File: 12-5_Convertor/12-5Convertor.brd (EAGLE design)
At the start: 29.1 x 41.3 mm, 14 parts, among them IC1 ACS764, U1 LM2678

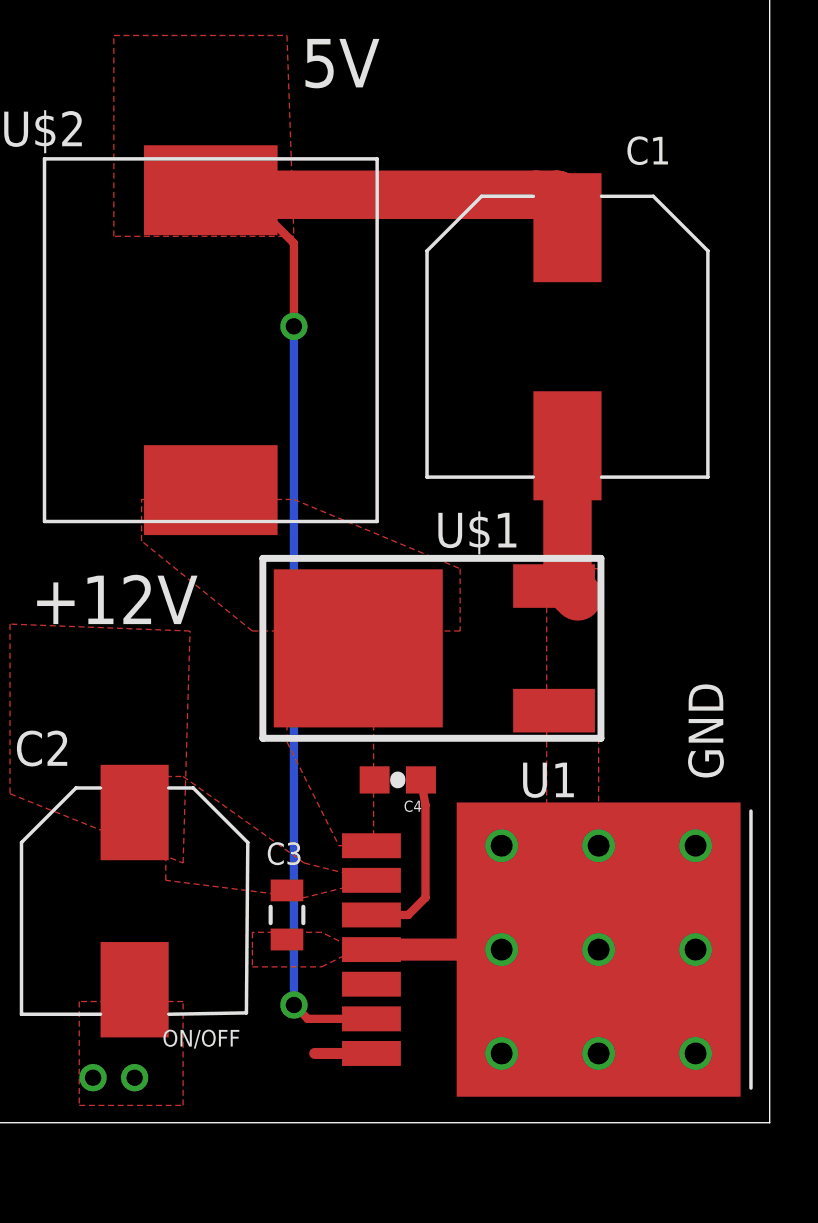
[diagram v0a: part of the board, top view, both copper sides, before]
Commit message: Cleaned up the buck regulator schematic
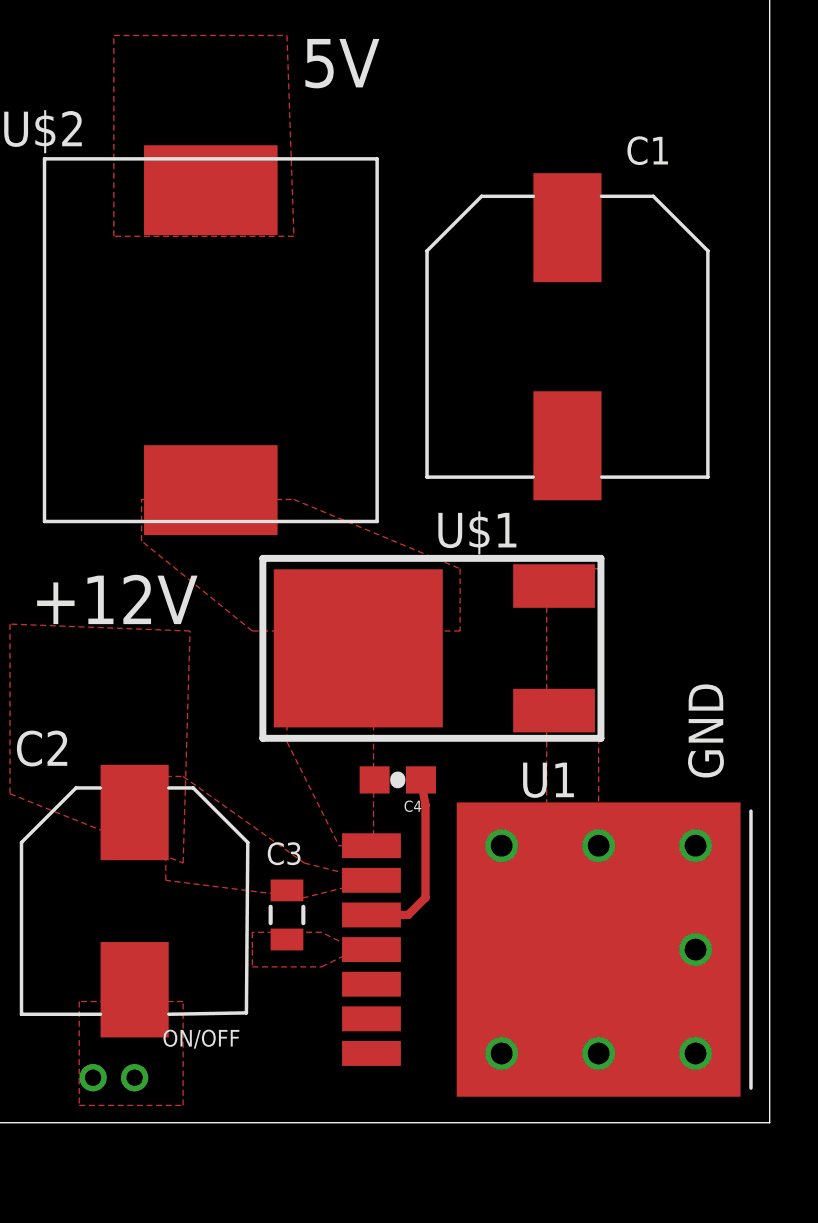
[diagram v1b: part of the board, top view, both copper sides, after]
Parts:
- C7, C8: value 10UF -> 1uF
- U$2: value HCMA1305 -> 22uH
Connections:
- removed net N$1: C8.1, R1.1, U$3.OUT
- new net N$5: R1.2, U1.7
- net +3V3: now also C8.1, R1.1, U$3.OUT; no longer R1.2, U1.7
- net +5V: no longer U1.6
- net VOUT: now also U1.6
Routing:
- net +5V: track 52.4 -> 0.00 mm, vias 2 -> 0
- net GND: track 10.5 -> 0.00 mm, vias 11 -> 9
- net +3V3: track 2.08 -> 0.00 mm

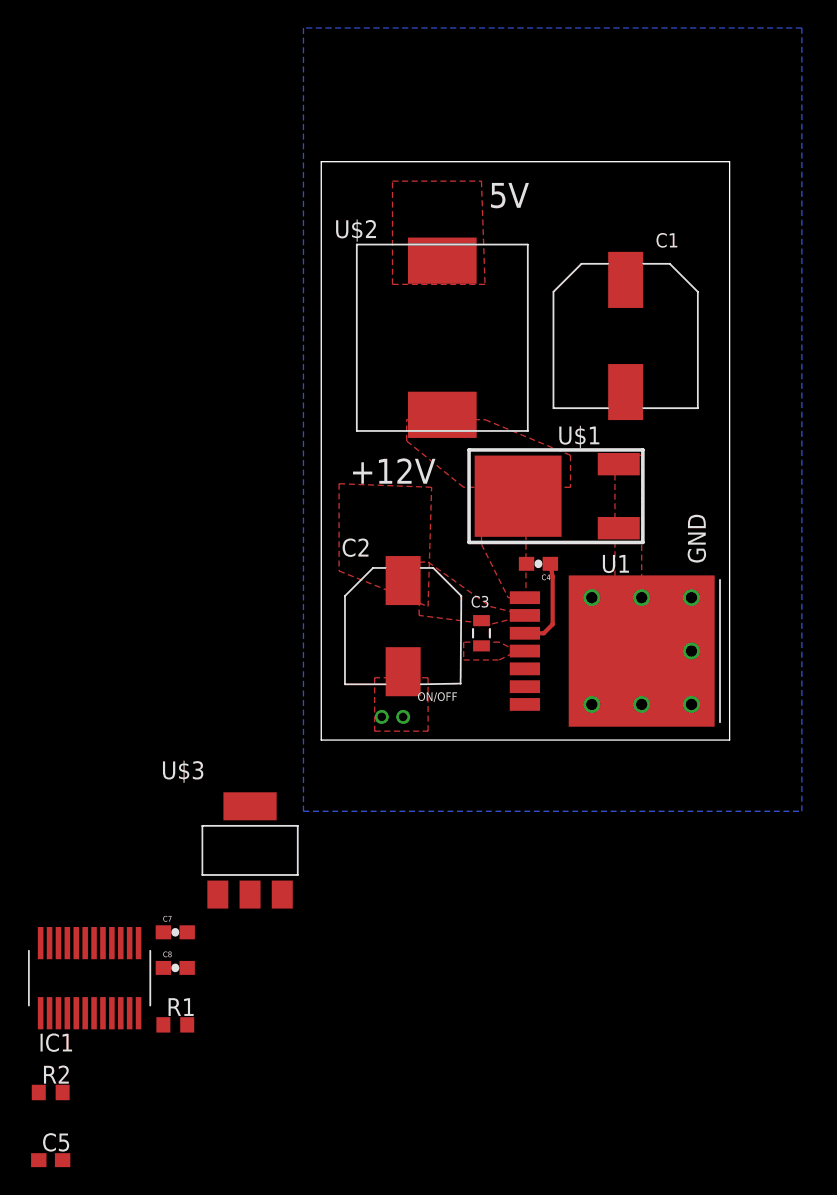
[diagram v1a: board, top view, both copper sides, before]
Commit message: ripped of wires in order to preapare for new board layout
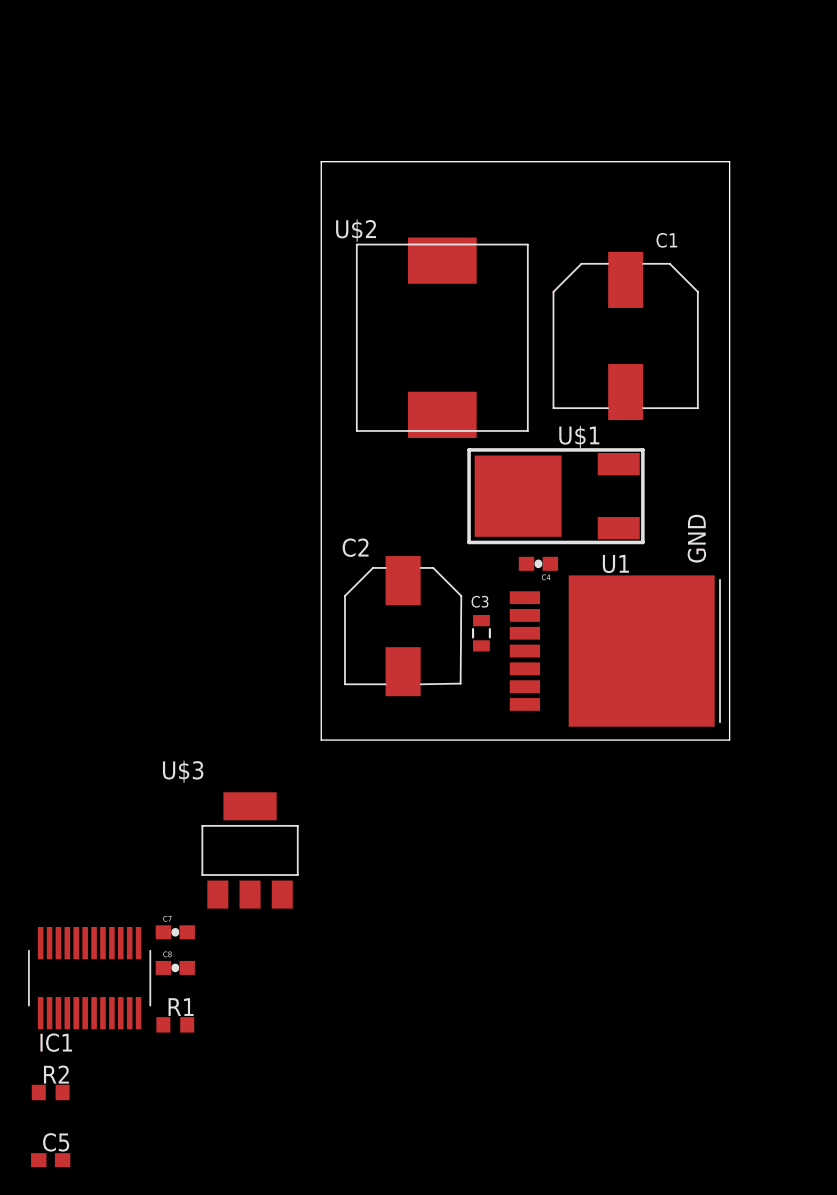
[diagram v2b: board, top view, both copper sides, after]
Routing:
- net N$2: track 6.58 -> 0.00 mm
- removed copper zone on layer 1, net +12V
- removed copper zone on layer 1, net +5V
- removed copper zone on layer 1, net GND
- removed copper zone on layer 16, net GND
- removed copper zone on layer 1, net N$3
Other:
- board text removed: "+12V"
- board text removed: "5V"
- board text removed: "ON/OFF"
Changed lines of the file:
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@@
 <?xml version="1.0" encoding="utf-8"?>
 <!DOCTYPE eagle SYSTEM "eagle.dtd">
-<eagle version="7.3.0">
+<eagle version="7.4.0">
 <drawing>
 <settings>
@@
 <grid distance="0.01" unitdist="inch" unit="inch" style="lines" multiple="1" display="yes" altdistance="0.025" altunitdist="inch" altunit="inch"/>
 <layers>
-<layer number="1" name="Top" color="4" fill="1" visible="no" active="yes"/>
-<layer number="16" name="Bottom" color="1" fill="1" visible="no" active="yes"/>
+<layer number="1" name="Top" color="4" fill="1" visible="yes" active="yes"/>
+<layer number="16" name="Bottom" color="1" fill="1" visible="yes" active="yes"/>
 <layer number="17" name="Pads" color="2" fill="1" visible="yes" active="yes"/>
 <layer number="18" name="Vias" color="2" fill="1" visible="yes" active="yes"/>
 <layer number="19" name="Unrouted" color="6" fill="1" visible="yes" active="yes"/>
 <layer number="20" name="Dimension" color="15" fill="1" visible="yes" active="yes"/>
-<layer number="21" name="tPlace" color="7" fill="1" visible="no" active="yes"/>
+<layer number="21" name="tPlace" color="7" fill="1" visible="yes" active="yes"/>
 <layer number="22" name="bPlace" color="7" fill="1" visible="yes" active="yes"/>
 <layer number="23" name="tOrigins" color="15" fill="1" visible="yes" active="yes"/>
@@
 <wire x1="60.884" y1="59.045" x2="31.75" y2="59.045" width="0" layer="20"/>
 <wire x1="31.75" y1="59.045" x2="31.75" y2="17.78" width="0" layer="20"/>
-<text x="33.782" y="36.068" size="1.778" layer="21">+12V</text>
-<text x="43.688" y="55.753" size="1.778" layer="21">5V</text>
 <text x="59.182" y="30.353" size="1.27" layer="21" rot="R90">GND</text>
-<text x="38.608" y="20.574" size="0.6096" layer="21">ON/OFF</text>
 <text x="37.846" y="54.102" size="1.016" layer="22" rot="MR180">Designed by Luke McBee,
 Richard Shen, Jeff Geiss,
@@
 <contactref element="U1" pad="3"/>
 <contactref element="C4" pad="1"/>
-<wire x1="46.2788" y1="25.4" x2="47.625" y2="25.4" width="0.3048" layer="1"/>
-<wire x1="47.625" y1="25.4" x2="48.26" y2="26.035" width="0.3048" layer="1"/>
-<wire x1="48.26" y1="26.035" x2="48.26" y2="29.425" width="0.3048" layer="1"/>
-<wire x1="48.26" y1="29.425" x2="48.094" y2="30.353" width="0.3048" layer="1"/>
+<wire x1="46.2788" y1="25.4" x2="48.094" y2="30.353" width="0" layer="19" extent="1-1"/>
 </signal>
 <signal name="N$3">
 <contactref element="C4" pad="2"/>
-<polygon width="0.4064" layer="1" thermals="no">
-<vertex x="43.18" y="31.75"/>
-<vertex x="45.085" y="27.94"/>
-<vertex x="46.355" y="27.94"/>
-<vertex x="46.355" y="32.385"/>
-<vertex x="43.18" y="32.385"/>
-</polygon>
-<polygon width="0.254" layer="1" thermals="no">
-<vertex x="37.846" y="40.64"/>
-<vertex x="43.434" y="40.64"/>
-<vertex x="49.53" y="38.1"/>
-<vertex x="49.53" y="35.814"/>
-<vertex x="41.91" y="35.814"/>
-<vertex x="37.846" y="39.116"/>
-</polygon>
 <contactref element="U1" pad="1"/>
 <contactref element="U$2" pad="P$1"/>
 <contactref element="U$1" pad="P$4"/>
-<wire x1="45.795" y1="35.179" x2="40.386" y2="40.982" width="0" layer="19" extent="1-1"/>
-<wire x1="46.394" y1="30.353" x2="45.795" y2="35.179" width="0" layer="19" extent="1-1"/>
-<wire x1="46.2788" y1="27.94" x2="46.394" y2="30.353" width="0" layer="19" extent="1-1"/>
 </signal>
 <signal name="GND">
-<via x="51.054" y="20.32" extent="1-16" drill="0.8"/>
-<via x="51.054" y="27.94" extent="1-16" drill="0.8"/>
-<via x="54.61" y="20.32" extent="1-16" drill="0.8"/>
-<via x="58.166" y="20.32" extent="1-16" drill="0.8"/>
-<via x="58.166" y="24.13" extent="1-16" drill="0.8"/>
-<via x="58.166" y="27.94" extent="1-16" drill="0.8"/>
-<via x="54.61" y="27.94" extent="1-16" drill="0.8"/>
-<via x="36.068" y="19.431" extent="1-16" drill="0.6"/>
-<polygon width="0.3048" layer="16">
-<vertex x="30.48" y="12.7"/>
-<vertex x="66.04" y="12.7"/>
-<vertex x="66.04" y="68.58"/>
-<vertex x="30.48" y="68.58"/>
-</polygon>
-<polygon width="0.3048" layer="1" thermals="no">
-<vertex x="52.705" y="38.1"/>
-<vertex x="52.705" y="29.21"/>
-<vertex x="54.61" y="29.21"/>
-<vertex x="54.61" y="38.1"/>
-</polygon>
-<polygon width="0.3048" layer="1" thermals="no">
-<vertex x="45.72" y="24.13"/>
-<vertex x="44.45" y="24.765"/>
-<vertex x="41.91" y="24.765"/>
-<vertex x="41.91" y="24.13"/>
-<vertex x="41.91" y="23.495"/>
-<vertex x="44.45" y="23.495"/>
-</polygon>
-<polygon width="0.3048" layer="1" thermals="no">
-<vertex x="35.56" y="22.225"/>
-<vertex x="35.56" y="18.415"/>
-<vertex x="39.37" y="18.415"/>
-<vertex x="39.37" y="22.225"/>
-</polygon>
-<via x="37.592" y="19.431" extent="1-16" drill="0.6"/>
 <contactref element="C7" pad="2"/>
 <contactref element="C8" pad="2"/>
@@
 <contactref element="IC1" pad="17"/>
 <wire x1="52.975" y1="37.464" x2="53.467" y2="42.609" width="0" layer="19" extent="1-1"/>
-<wire x1="52.975" y1="32.894" x2="52.975" y2="37.464" width="0" layer="19" extent="1-1"/>
-<wire x1="54.61" y1="27.94" x2="52.975" y2="32.894" width="0" layer="19" extent="1-1"/>
-<wire x1="58.166" y1="27.94" x2="54.61" y2="27.94" width="0" layer="19" extent="1-1"/>
-<wire x1="51.054" y1="27.94" x2="54.61" y2="27.94" width="0" layer="19" extent="1-1"/>
-<wire x1="58.166" y1="24.13" x2="58.166" y2="27.94" width="0" layer="19" extent="1-1"/>
-<wire x1="54.61" y1="24.13" x2="58.166" y2="24.13" width="0" layer="19" extent="1-1"/>
-<wire x1="58.166" y1="20.32" x2="58.166" y2="24.13" width="0" layer="19" extent="1-1"/>
-<wire x1="54.61" y1="20.32" x2="58.166" y2="20.32" width="0" layer="19" extent="1-1"/>
-<wire x1="51.054" y1="20.32" x2="54.61" y2="20.32" width="0" layer="19" extent="1-1"/>
-<wire x1="46.2788" y1="24.13" x2="51.054" y2="27.94" width="0" layer="19" extent="1-1"/>
+<wire x1="46.2788" y1="24.13" x2="54.61" y2="24.13" width="0" layer="19" extent="1-1"/>
 <wire x1="43.18" y1="24.5" x2="46.2788" y2="24.13" width="0" layer="19" extent="1-1"/>
 <wire x1="37.592" y1="22.658" x2="43.18" y2="24.5" width="0" layer="19" extent="1-1"/>
-<wire x1="37.592" y1="19.431" x2="37.592" y2="22.658" width="0" layer="19" extent="1-1"/>
-<wire x1="36.068" y1="19.431" x2="37.592" y2="19.431" width="0" layer="19" extent="1-1"/>
-<wire x1="24.37" y1="6.756" x2="36.068" y2="19.431" width="0" layer="19" extent="1-1"/>
+<wire x1="24.37" y1="6.756" x2="37.592" y2="22.658" width="0" layer="19" extent="1-1"/>
 <wire x1="22.186" y1="4.064" x2="24.37" y2="6.756" width="0" layer="19" extent="1-1"/>
 <wire x1="22.186" y1="1.524" x2="22.186" y2="4.064" width="0" layer="19" extent="1-1"/>
@@
 </signal>
 <signal name="+12V">
-<polygon width="0.254" layer="1" thermals="no">
-<vertex x="39.37" y="30.48"/>
-<vertex x="43.815" y="27.305"/>
-<vertex x="46.355" y="26.67"/>
-<vertex x="43.815" y="26.035"/>
-<vertex x="38.735" y="26.67"/>
-<vertex x="38.735" y="30.48"/>
-</polygon>
-<polygon width="0.254" layer="1" thermals="no">
-<vertex x="39.37" y="27.305"/>
-<vertex x="39.624" y="35.814"/>
-<vertex x="33.02" y="36.068"/>
-<vertex x="33.02" y="29.845"/>
-</polygon>
 <contactref element="U$3" pad="INPUT"/>
 <contactref element="C7" pad="1"/>
@@
 <contactref element="U1" pad="2"/>
 <contactref element="C3" pad="1"/>
-<wire x1="43.18" y1="26.3" x2="46.2788" y2="26.67" width="0" layer="19" extent="1-1"/>
-<wire x1="37.592" y1="29.158" x2="43.18" y2="26.3" width="0" layer="19" extent="1-1"/>
-<wire x1="28.97" y1="6.756" x2="37.592" y2="29.158" width="0" layer="19" extent="1-1"/>
 <wire x1="20.486" y1="4.064" x2="28.97" y2="6.756" width="0" layer="19" extent="1-1"/>
+<wire x1="37.592" y1="29.158" x2="28.97" y2="6.756" width="0" layer="19" extent="1-1"/>
 </signal>
 <signal name="+5V">
-<polygon width="0.3048" layer="1" thermals="no">
-<vertex x="36.83" y="57.658"/>
-<vertex x="43.18" y="57.658"/>
-<vertex x="43.434" y="50.292"/>
-<vertex x="36.83" y="50.292"/>
-</polygon>
 <contactref element="IC1" pad="19"/>
 <contactref element="IC1" pad="18"/>

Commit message: Updated the power conversion board
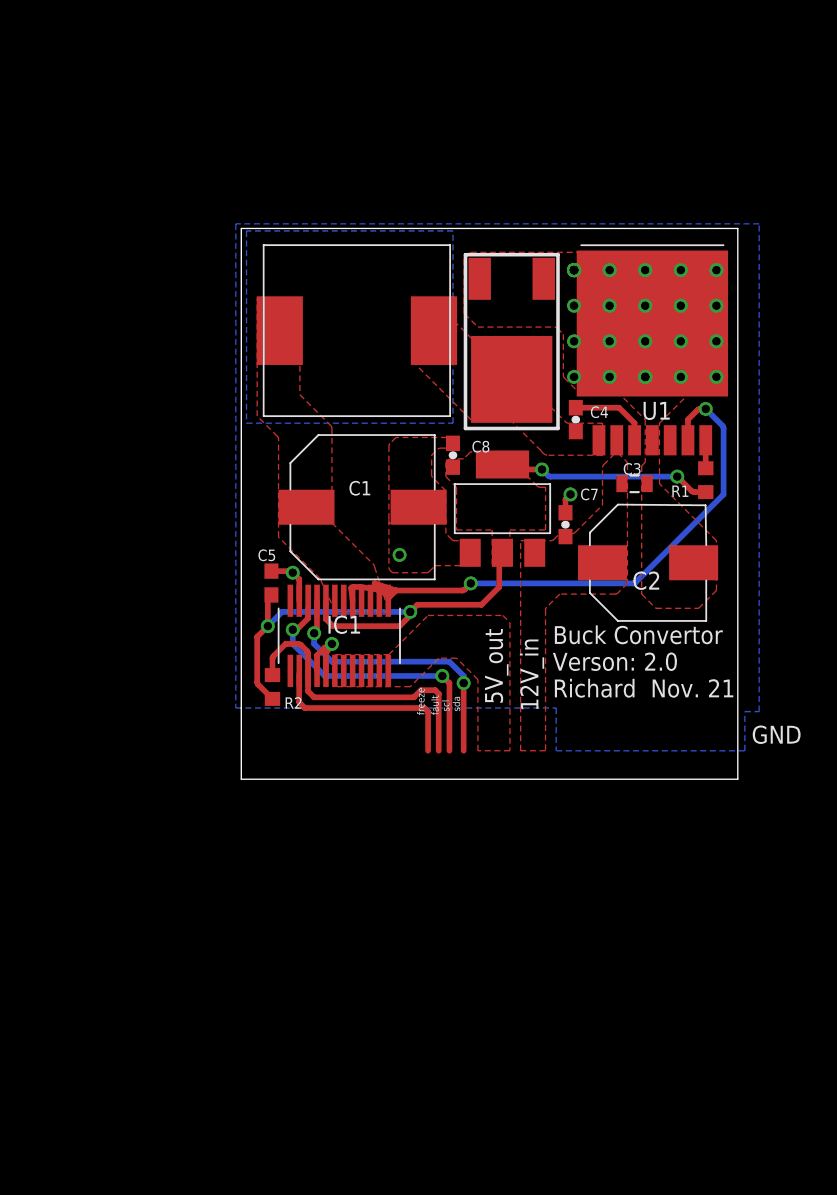
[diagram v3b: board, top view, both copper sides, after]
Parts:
- R1: value 1kOhm -> 10Ω
- moved R1 54.2 mm to (59.2, 36.3), turned to 90 degrees
- moved C5 44.1 mm to (28.2, 29.0), turned to 90 degrees
- moved C8 41.6 mm to (41.1, 38.1), turned to 90 degrees
- moved C7 40.3 mm to (49.2, 33.1), turned to 90 degrees
- moved R2 33.0 mm to (28.3, 21.6), turned to 270 degrees
- moved U$3 30.3 mm to (44.7, 34.3)
- moved IC1 30.3 mm to (33.0, 25.2), turned to 180 degrees
- moved U1 23.4 mm to (55.4, 47.5), turned to 270 degrees
- moved C1 22.4 mm to (34.7, 34.4), turned to 90 degrees
- moved C2 18.1 mm to (55.1, 30.4), turned to 90 degrees
- moved C3 15.3 mm to (54.1, 36.1), turned to 0 degrees
- moved U$1 12.0 mm to (45.3, 46.6), turned to 90 degrees
- moved C4 10.6 mm to (49.9, 40.6), turned to 270 degrees
- moved U$2 6.12 mm to (34.3, 47.0), turned to 270 degrees
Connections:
- net +3V3: now also U$3.TAB
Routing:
- net +3V3: track 0.00 -> 51.8 mm, vias 0 -> 4
- net VOUT: track 0.00 -> 43.7 mm, vias 0 -> 2
- net SCL: track 0.00 -> 20.3 mm, vias 0 -> 2
- net SDA: track 0.00 -> 20.1 mm, vias 0 -> 2
- net N$6: track 0.00 -> 15.3 mm
- net N$7: track 0.00 -> 14.3 mm
- net GND: track 0.00 -> 9.77 mm, vias 0 -> 28
- net N$2: track 0.00 -> 5.87 mm
- net FAULT: track 0.00 -> 5.74 mm
- net N$5: track 0.00 -> 1.99 mm
- added copper zone on layer 1, net +12V
- added copper zone on layer 1, net +3V3
- added copper zone on layer 1, net +5V
- added copper zone on layer 1, net GND
- added copper zone on layer 16, net GND
- added copper zone on layer 1, net N$3
- added copper zone on layer 16, net N$8
- added copper zone on layer 1, net VOUT
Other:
- board size 29.1 x 41.3 mm -> 35.4 x 39.3 mm
- board text added: "12V_in"
- board text added: "5V_out"
- board text added: "Buck Convertor Verson: 2.0 Richard Nov. 21"
- board text added: "GND loop?"
- board text added: "fault"
- board text added: "freeze"
- board text added: "scl"
- board text added: "sda"
- board text removed: "Designed by Luke McBee, Richard Shen, Jeff Geiss, and Dimcho Karakashev +12V to +5V Buck Regulator 11/8/2015"
